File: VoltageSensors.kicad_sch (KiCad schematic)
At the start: 9 parts

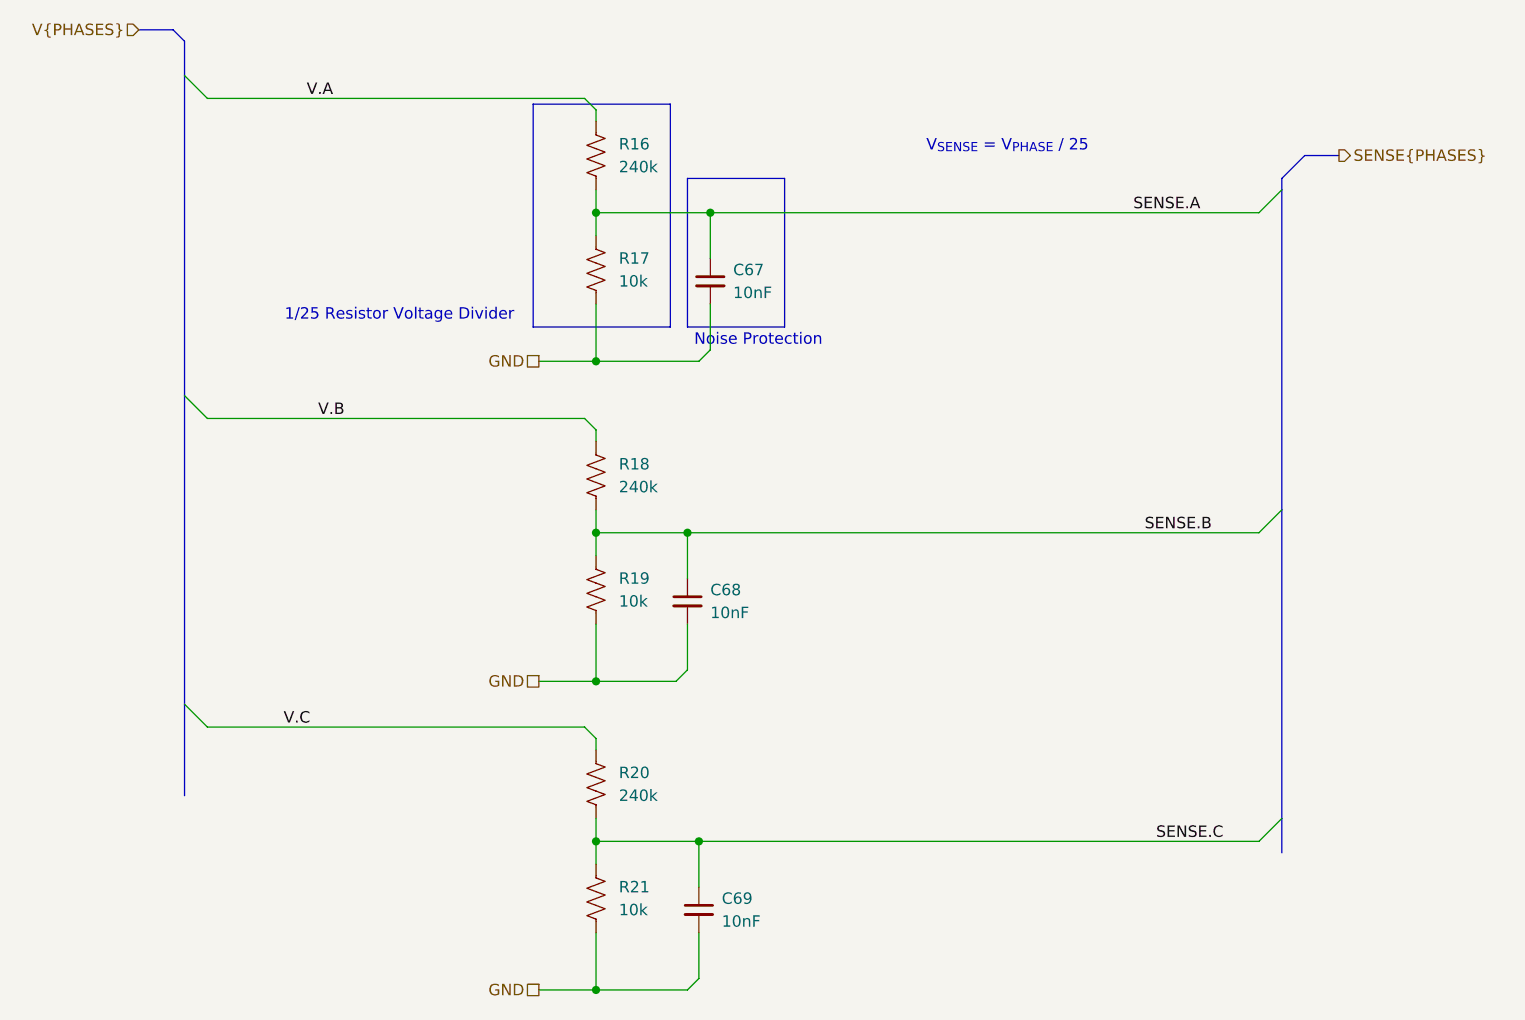
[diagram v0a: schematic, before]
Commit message: added more capacitance
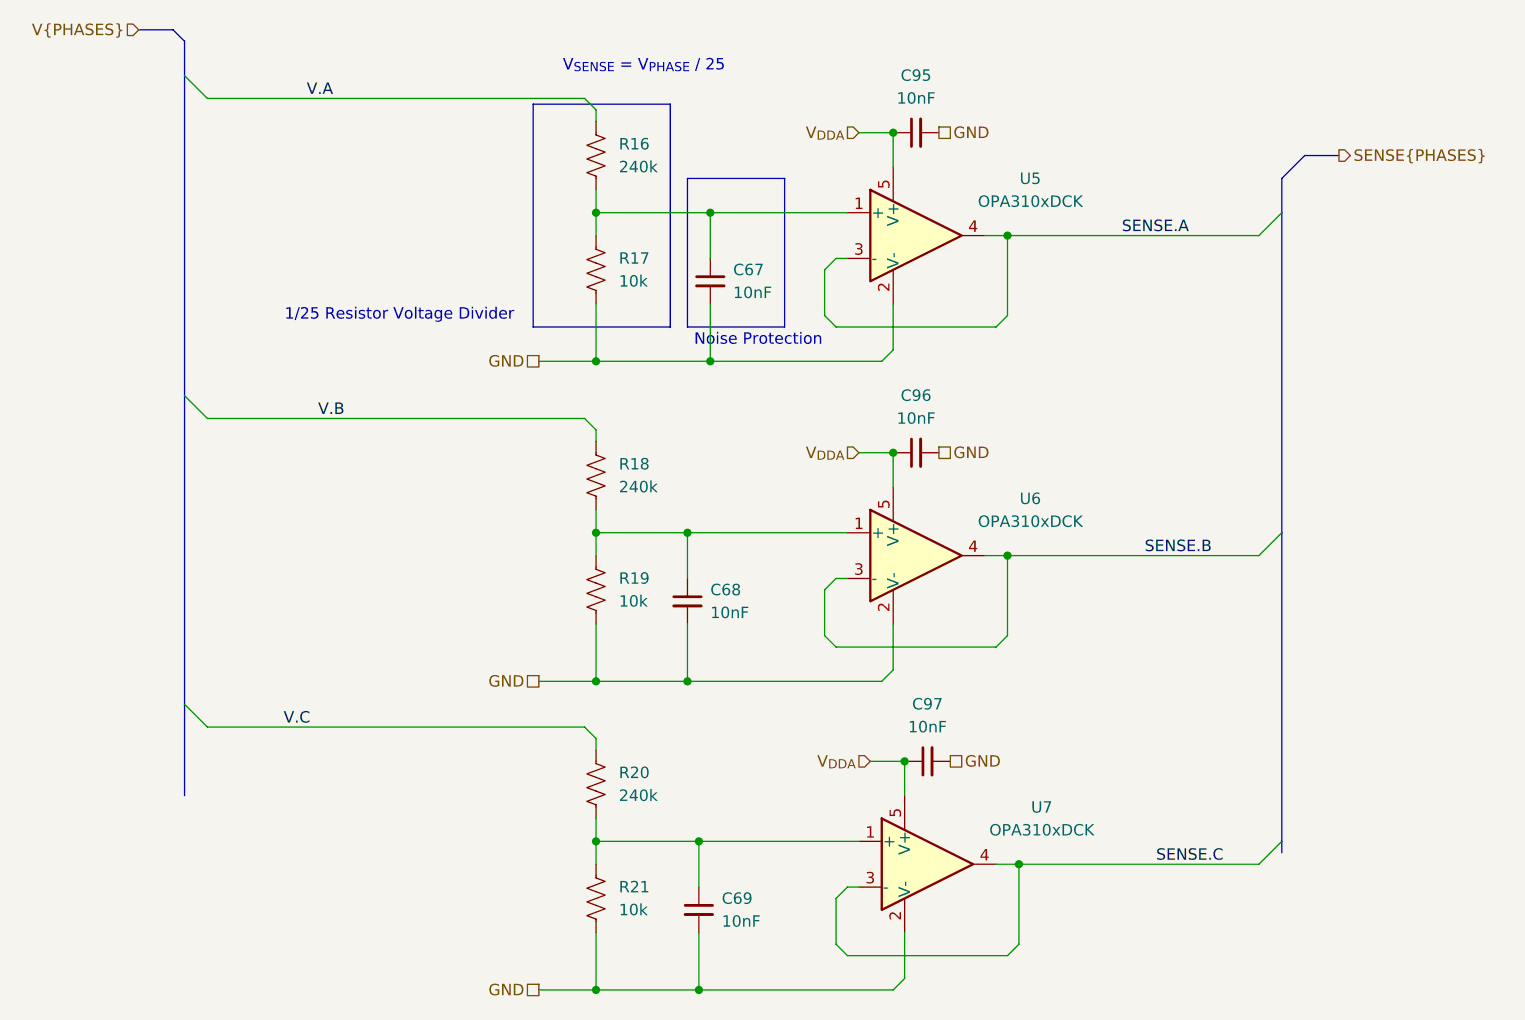
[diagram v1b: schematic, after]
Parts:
- added C95, C96, C97: 10nF, OpenMD:C_0402_1005Metric, symbol OpenMD:C_Small
- added U5, U6, U7: OPA310xDCK, OpenMD:SOT-353_SC-70-5, symbol OpenMD:OPA310xDCK
- C67, C68, C69: footprint Capacitor_SMD:C_0402_1005Metric -> OpenMD:C_0402_1005Metric; symbol Device:C_Small -> OpenMD:C_Small
- R16, R17, R18, R19, R20, R21: footprint Resistor_SMD:R_0402_1005Metric -> OpenMD:R_0402_1005Metric; symbol Device:R_US -> OpenMD:R_US
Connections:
- net GND: now also C95.2, C96.2, C97.2, U5.2 (V-), U6.2 (V-), U7.2 (V-)
- net SENSE.A: now also U5.3 (-), U5.4; no longer C67.1, R16.2, R17.1
- net SENSE.B: now also U6.3 (-), U6.4; no longer C68.1, R18.2, R19.1
- net SENSE.C: now also U7.3 (-), U7.4; no longer C69.1, R20.2, R21.1
- new net: C67.1, R16.2, R17.1, U5.1 (+)
- new net: C68.1, R18.2, R19.1, U6.1 (+)
- new net: C69.1, R20.2, R21.1, U7.1 (+)
- new net V_{DDA}: C95.1, C96.1, C97.1, U5.5 (V+), U6.5 (V+), U7.5 (V+)
